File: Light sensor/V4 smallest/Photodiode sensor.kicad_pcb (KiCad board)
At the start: 2 copper layers, 28.5 x 24 mm, 20 parts, among them IC1 BH1730FVC-TR, J1 Conn_01x02, J2 Conn_01x04, J2 Conn_01x05, J3 Conn_01x04, J3 Conn_01x05

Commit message: V4 PCB update
Had to use a backup
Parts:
- removed C2: C1608X5R1E475K080AC, CUSTOM_LIBRARY:CAPC1608X80N
- removed C7: KAM21BR71H104JM, CUSTOM_LIBRARY:CAPC2012X94N
- removed the J1 at (121.2, 95.1)
- removed the J1 at (134.2, 122.4)
- removed the J2 at (126.8, 97.5)
- removed the J2 at (120.9, 86.8)
- removed the J3 at (121.1, 100.8)
- removed the J3 at (130.2, 97.5)
- removed LED1: LTR-390UV-01, CUSTOM_LIBRARY:LTR390UV01
- removed the R5 at (109.9, 97.9)
- removed the R5 at (105.1, 92.2)
- removed the R6 at (112.5, 95.0)
- removed the R6 at (113.5, 102.3)
- removed the R7 at (108.3, 105.0)
- removed the R7 at (102.2, 95.2)
- added J1: Conn_01x02, Connector_PinHeader_1.00mm:PinHeader_1x02_P1.00mm_Vertical, F.Cu at (166.9, 113.8)
- added J2: Conn_01x04, Connector_PinHeader_1.00mm:PinHeader_1x04_P1.00mm_Vertical, F.Cu at (166.9, 107.3)
- added J3: Conn_01x05, Connector_PinHeader_1.00mm:PinHeader_1x05_P1.00mm_Vertical, F.Cu at (167.0, 118.6)
- added R5: ERJHP6J821V, CUSTOM_LIBRARY:ERJHP6D1000V, F.Cu at (158.8, 115.6)
- added R6: ERJHP6J821V, CUSTOM_LIBRARY:ERJHP6D1000V, F.Cu at (162.4, 120.0)
- added R7: RC0402JR-073M3L, CUSTOM_LIBRARY:ERJHP6D1000V, F.Cu at (157.3, 122.7)
- moved R3 61.5 mm to (156.6, 112.6), turned to 180 degrees
- moved IC1 52.1 mm to (159.3, 109.0)
- moved R1 52.0 mm to (161.8, 112.1)
- moved D5 52.0 mm to (159.2, 125.6)
- moved R2 52.0 mm to (161.8, 105.8)
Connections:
- net /INT renamed /INT 2
- IC1 pad 4: /SDA -> /SDA 2
- IC1 pad 6: /SCL -> /SCL 2
- R1 pad 1: /SCL -> /SCL 2
- R2 pad 1: /SDA -> /SDA 2
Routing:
- net /INT 2: track 0.00 -> 13.7 mm, vias 0 -> 1
- net /READY: track 1.11 -> 13.4 mm
- net /SYN: track 1.38 -> 13.5 mm
- net /SCL 2: track 0.00 -> 6.67 mm, vias 0 -> 1
- net /SDA: track 4.47 -> 10.8 mm
- net /SDA 2: track 0.00 -> 6.28 mm, vias 0 -> 1
- net /SCL: track 4.50 -> 8.61 mm
- net /3.3V: track 5.67 -> 7.78 mm, vias 4 -> 7
- net GND: track 7.01 -> 7.72 mm, vias 7 -> 8
- added copper zone on In1.Cu, net GND
- added copper zone on In2.Cu, net GND
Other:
- board size 28.5 x 24 mm -> 16.3 x 19.2 mm
- copper layers 2 -> 4

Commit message: Updated footprints
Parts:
- added C1: KAM21BR71H104JM, CUSTOM_LIBRARY:CAPC2012X94N, F.Cu at (164.7, 114.0)
- added C2: C1608X5R1E475K080AC, CUSTOM_LIBRARY:CAPC1608X80N, F.Cu at (166.1, 116.6)
- R1, R2, R3: value RC0402JR-073M3L -> RMCA1206FT4K70-HP; footprint CUSTOM_LIBRARY:RC0402JR-073M3L -> CUSTOM_LIBRARY:RMCA1206FT4K70-HP
- moved R3 10.4 mm to (165.6, 107.4), turned to -90 degrees
- moved R1 8.99 mm to (155.3, 105.9), turned to 0 degrees
- moved R2 7.42 mm to (165.6, 112.2), turned to -90 degrees
- moved IC1 1.23 mm to (160.2, 109.9)
- moved J2 0.89 mm to (166.9, 108.2)
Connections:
- R1 pad 1: /SCL 2 -> /INT 2
- R3 pad 1: /INT 2 -> /SCL 2
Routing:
- net /INT 2: track 13.7 -> 3.46 mm, vias 1 -> 0
- net /3.3V: track 7.78 -> 15.0 mm, vias 7 -> 9
- net /SCL 2: track 6.67 -> 7.86 mm
- net /SDA 2: track 6.28 -> 7.30 mm

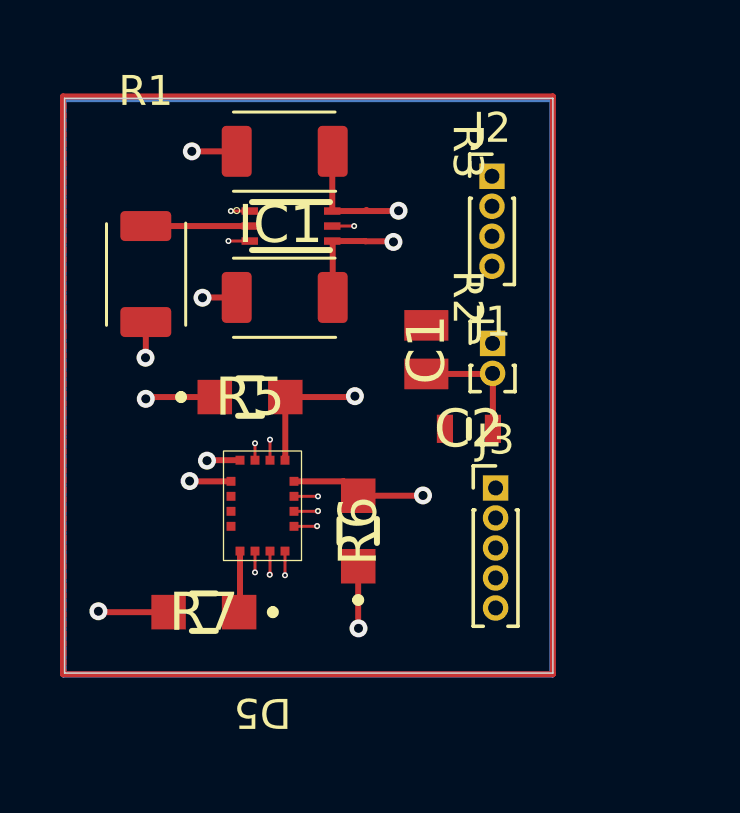
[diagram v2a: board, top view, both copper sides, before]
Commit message: Changed V4 PCB
Connected both SCL and SDA pins together as they have different addresses. Made the PCB a lot smaller. Got a good connector placed on the bottom side of the PCB
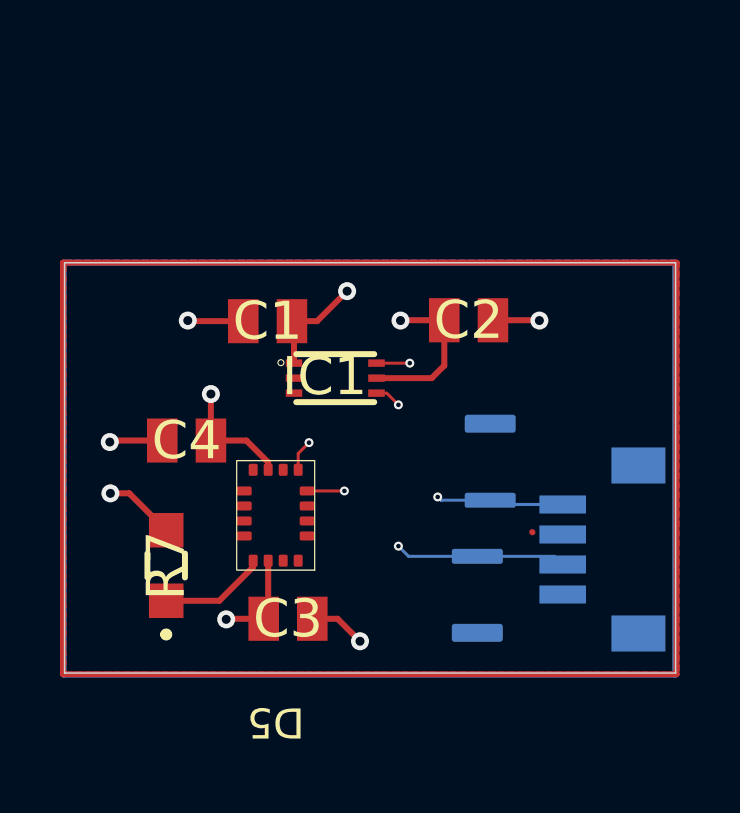
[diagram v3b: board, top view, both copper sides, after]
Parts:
- removed J2: Conn_01x04, Connector_PinHeader_1.00mm:PinHeader_1x04_P1.00mm_Vertical
- removed J3: Conn_01x05, Connector_PinHeader_1.00mm:PinHeader_1x05_P1.00mm_Vertical
- removed R1: RMCA1206FT4K70-HP, CUSTOM_LIBRARY:RMCA1206FT4K70-HP
- removed R5, R6: ERJHP6J821V, CUSTOM_LIBRARY:ERJHP6D1000V
- added C3: KAM21BR71H104JM, CUSTOM_LIBRARY:CAPC2012X94N, F.Cu at (160.1, 123.0)
- added C4: KAM21BR71H104JM, CUSTOM_LIBRARY:CAPC2012X94N, F.Cu at (156.7, 117.0)
- C2: value C1608X5R1E475K080AC -> KAM21BR71H104JM; footprint CUSTOM_LIBRARY:CAPC1608X80N -> CUSTOM_LIBRARY:CAPC2012X94N
- J1: value Conn_01x02 -> BM04B-SRSS-TB_LF__SN_; footprint Connector_PinHeader_1.00mm:PinHeader_1x02_P1.00mm_Vertical -> CUSTOM_LIBRARY:BM04B-SRSS-TB_LFSN_; moved to B.Cu
- R2, R3: moved to B.Cu
- moved R3 15.8 mm to (166.8, 123.2), turned to 0 degrees
- moved J1 10.3 mm to (169.7, 123.6), turned to 90 degrees
- moved C1 5.37 mm to (159.4, 113.0), turned to 180 degrees
- moved IC1 5.28 mm to (161.6, 114.9)
- moved R2 4.55 mm to (166.4, 116.7), turned to 180 degrees
- moved C2 3.62 mm to (166.1, 113.0), turned to 0 degrees
- moved R7 2.00 mm to (156.0, 121.2), turned to 90 degrees
- moved D5 0.54 mm to (159.7, 125.9)
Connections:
- D5 pad 9: /READY -> unconnected-(D5-READY-Pad9)
- IC1 pad 4: /SDA 2 -> /SDA
- IC1 pad 6: /SCL 2 -> /SCL
- J1 pad 1: GND -> /3.3V
- J1 pad 2: /3.3V -> /SDA
- R2 pad 1: /SDA 2 -> /SDA
- R3 pad 1: /SCL 2 -> /SCL
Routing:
- net /SYN: track 13.5 -> 0.00 mm, vias 1 -> 0
- net /READY: track 13.4 -> 0.00 mm, vias 1 -> 0
- net /SCL 2: track 7.86 -> 0.00 mm, vias 1 -> 0
- net /SDA 2: track 7.30 -> 0.00 mm, vias 1 -> 0
- net /SCL: track 8.61 -> 14.7 mm, vias 1 -> 3
- net /SDA: track 10.8 -> 15.9 mm, vias 1 -> 3
- net /INT 2: track 3.46 -> 0.00 mm
- net GND: track 7.72 -> 9.47 mm, vias 8 -> 5
- net Net-(D5-REXT): track 2.05 -> 3.57 mm
- net /3.3V: track 15.0 -> 16.4 mm, vias 9 -> 4
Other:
- board size 16.3 x 19.2 mm -> 20.4 x 13.7 mm

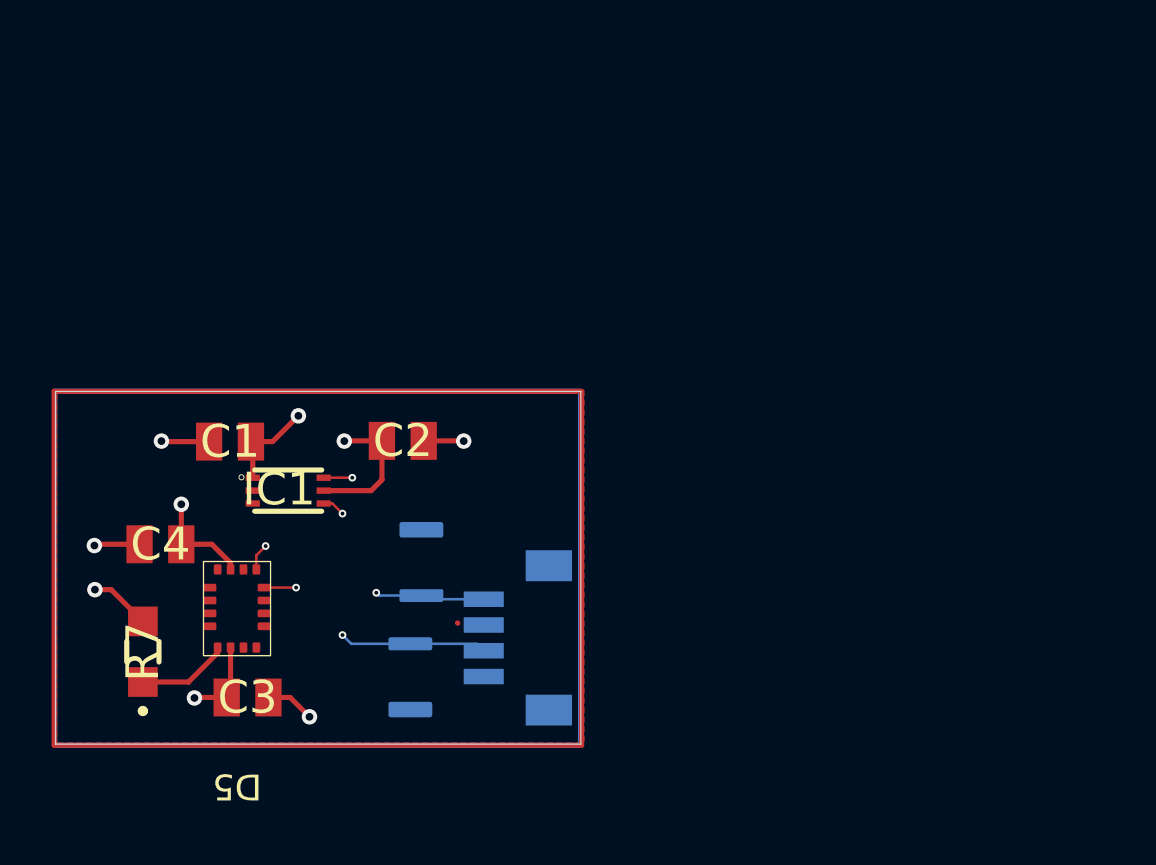
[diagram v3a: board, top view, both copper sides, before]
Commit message: Updated PCB components
Found in stock components and put onto the PCB. Need to double check against datasheet to ensure all connections are good
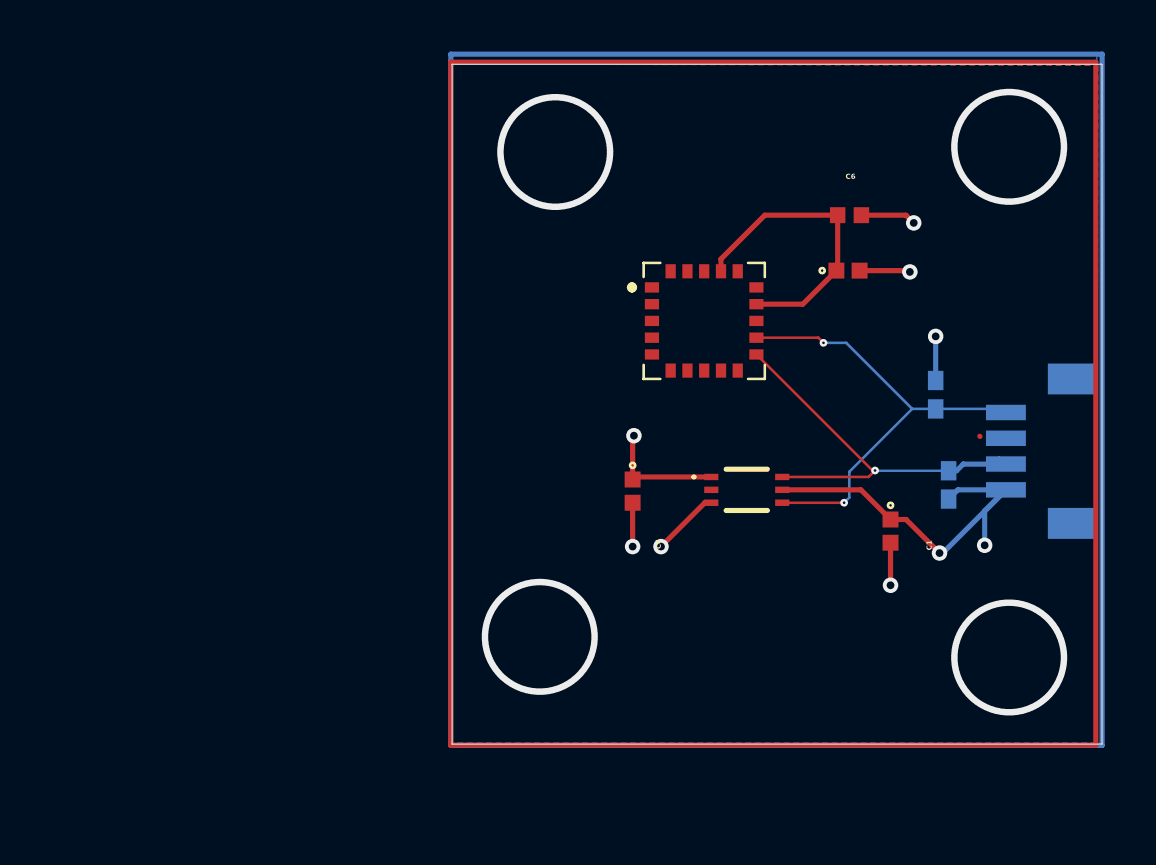
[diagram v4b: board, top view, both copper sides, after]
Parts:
- removed C2, C3: KAM21BR71H104JM, CUSTOM_LIBRARY:CAPC2012X94N
- removed D5: ~, CUSTOM_LIBRARY:AS7331-AQFM
- removed R2, R3: RMCA1206FT4K70-HP, CUSTOM_LIBRARY:RMCA1206FT4K70-HP
- removed R7: RC0402JR-073M3L, CUSTOM_LIBRARY:ERJHP6D1000V
- added C5: C0402C104M4PACTU, CUSTOM_LIBRARY:C0402, F.Cu at (183.3, 106.4)
- added C6: GRM155R61E105KA12D, CUSTOM_LIBRARY:CAPC1005X70N, F.Cu at (183.4, 104.2)
- added IC2: AS72653-BLGT, CUSTOM_LIBRARY:AS72651BLGT, F.Cu at (177.5, 108.3)
- added R1: MCWR04X4701FTL, CUSTOM_LIBRARY:RESC1005X40N, B.Cu at (187.2, 114.7)
- added R4: MCWR04X4701FTL, CUSTOM_LIBRARY:RESC1005X40N, B.Cu at (186.8, 111.2)
- C1, C4: value KAM21BR71H104JM -> C0402C104M4PACTU; footprint CUSTOM_LIBRARY:CAPC2012X94N -> CUSTOM_LIBRARY:C0402
- IC1: footprint CUSTOM_LIBRARY:WSOF6 -> CUSTOM_LIBRARY:BH1730FVCTR
- moved C1 25.8 mm to (185.0, 116.5), turned to -90 degrees
- moved J1 21.5 mm to (189.9, 116.4)
- moved C4 18.4 mm to (175.0, 115.0), turned to -90 degrees
- moved IC1 17.8 mm to (179.4, 114.9), turned to -90 degrees
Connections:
- J1 pad 2: /SDA -> /SCL
- J1 pad 4: /SCL -> /SDA
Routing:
- net Net-(IC2-VDD1): track 0.00 -> 11.5 mm
- net /3.3V: track 16.4 -> 22.1 mm
- net Net-(D5-REXT): track 3.57 -> 0.00 mm
- net /SDA: track 15.9 -> 18.0 mm, vias 3 -> 2
- net /SCL: track 14.7 -> 15.7 mm, vias 3 -> 1
- net GND: track 9.47 -> 10.1 mm, vias 5 -> 9
- added copper zone on In1.Cu, net /3.3V
- added copper zone on In2.Cu, net /3.3V
- added copper zone on B.Cu, net GND
- removed copper zone on B.Cu, net /3.3V
- removed copper zone on In1.Cu, net GND
- removed copper zone on In2.Cu, net GND
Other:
- board size 20.4 x 13.7 mm -> 25.2 x 26.4 mm

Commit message: Updated power connections
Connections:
- C5 pad 1: Net-(IC2-VDD1) -> /3.3V
- C6 pad 1: Net-(IC2-VDD1) -> /3.3V
- IC2 pad 14: Net-(IC2-VDD1) -> /3.3V
- IC2 pad 17: Net-(IC2-VDD1) -> /3.3V
- IC2 pad 8: unconnected-(IC2-I2C_ENB-Pad8) -> /3.3V
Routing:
- net /3.3V: track 22.1 -> 35.0 mm, vias 4 -> 5
- net Net-(IC2-VDD1): track 11.5 -> 0.00 mm
